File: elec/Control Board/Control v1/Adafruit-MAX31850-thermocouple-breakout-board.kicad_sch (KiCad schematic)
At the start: 20 parts

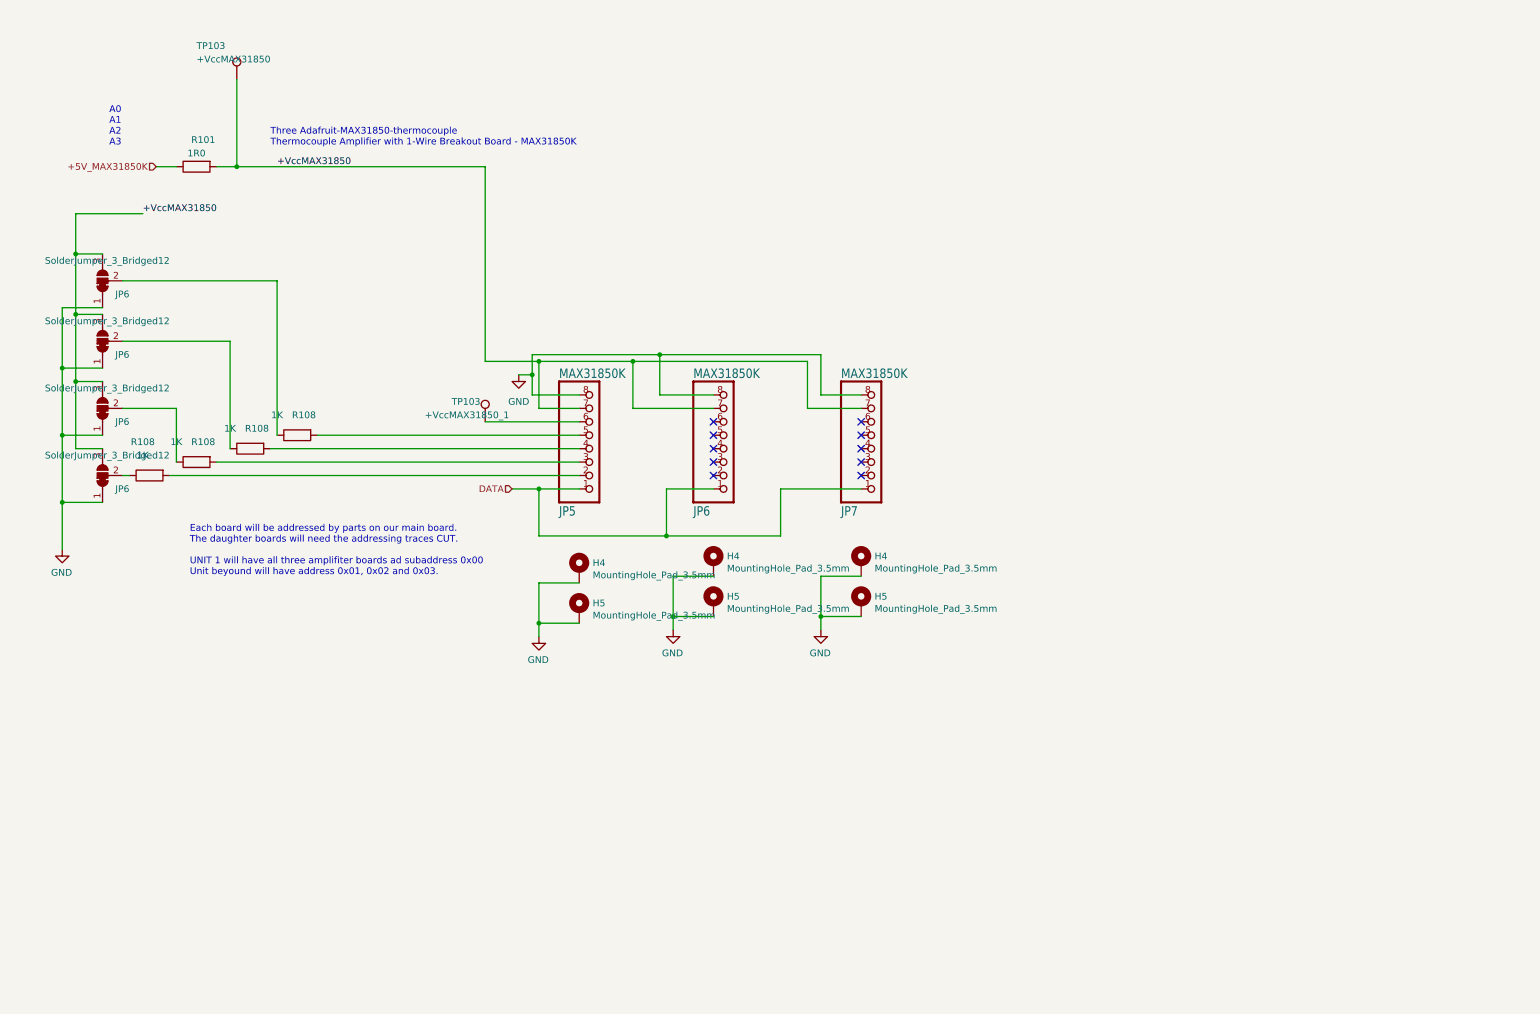
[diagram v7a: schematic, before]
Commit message: Update schematic for MCP9600 I2C thermocouple.
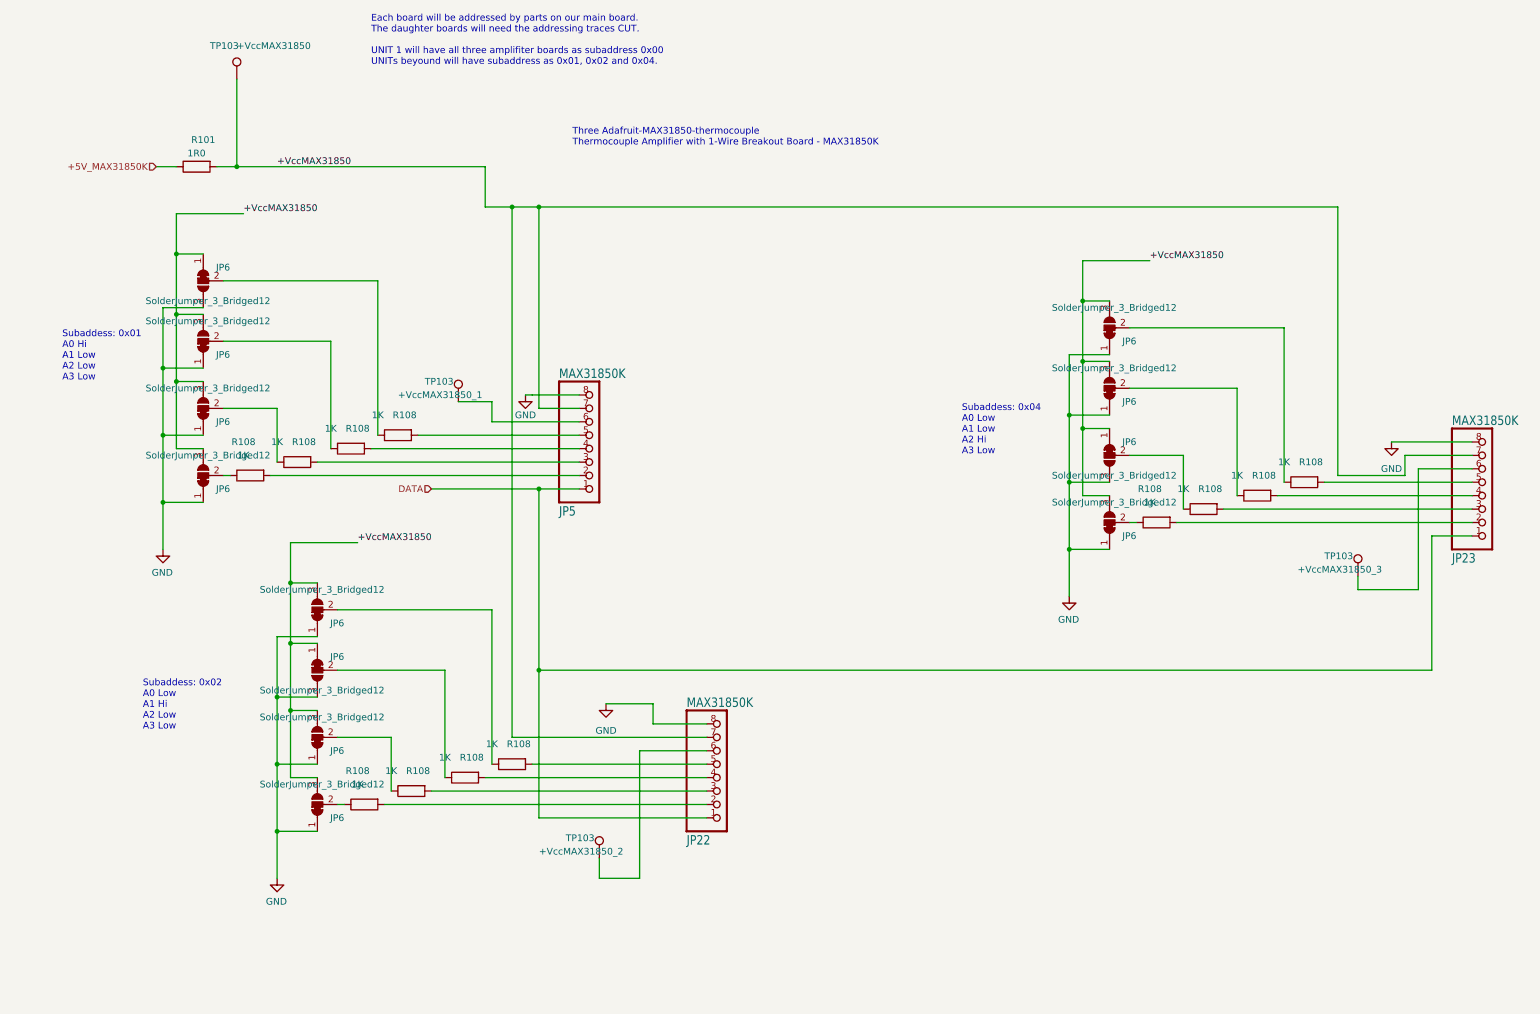
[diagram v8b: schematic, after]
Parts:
- removed H4 (x3), H5 (x3): MountingHole_Pad_3.5mm, PubInv_KiCad_PCB:MountingHole_3.5mm_Pad_Via, symbol GPAD_SCH_LIB:MountingHole_Pad_3.5mm
- removed JP6, JP7: MAX31850K, PubInv_KiCad_PCB:Adafruit_MAX31850K_Module, symbol Control v1-eagle-import:microbuilder_HEADER-1X870MIL
- added JP22, JP23: MAX31850K, PubInv_KiCad_PCB:Adafruit_MAX31850K_Module, symbol Control v1-eagle-import:microbuilder_HEADER-1X870MIL
- added JP6 (x8): SolderJumper_3_Bridged12, Jumper:SolderJumper-3_P1.3mm_Bridged12_RoundedPad1.0x1.5mm, symbol Jumper:SolderJumper_3_Bridged12
- added R108 (x8): 1K, Resistor_SMD:R_0603_1608Metric_Pad0.98x0.95mm_HandSolder, symbol Device:R
- added TP103: +VccMAX31850_2, TestPoint:TestPoint_Loop_D2.54mm_Drill1.5mm_Beaded, symbol Connector:TestPoint
- added TP103: +VccMAX31850_3, TestPoint:TestPoint_Loop_D2.54mm_Drill1.5mm_Beaded, symbol Connector:TestPoint
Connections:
- net +VccMAX31850: now also JP6.1 (A), JP22.7, JP23.7, JP6.1 (A), JP6.1 (A), JP6.3 (B), JP6.3 (B), JP6.3 (B), JP6.3 (B), JP6.3 (B), JP6.3 (B); no longer JP6.3 (B)
- net DATA: now also JP22.1, JP23.1
- net GND: now also JP6.3 (B), JP22.8, JP23.8, JP6.1 (A), JP6.1 (A), JP6.1 (A), JP6.1 (A), JP6.1 (A), JP6.1 (A), JP6.3 (B), JP6.3 (B); no longer JP6.1 (A)
- new net: JP6.2 (C), R108.1 (x8)
- new net: JP23.5, R108.2
- new net: JP23.4, R108.2
- new net: JP23.2, R108.2
- new net: JP22.6, TP103.1
- new net: JP22.5, R108.2
- new net: JP23.6, TP103.1
- new net: JP23.3, R108.2
- new net: JP22.4, R108.2
- new net: JP22.2, R108.2
- new net: JP22.3, R108.2
- no-connect marks 10 -> 0
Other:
- note added: "Each board will be addressed by parts on our main board. The daughter boards will need the addressing traces CUT. UNIT 1 will have all three amplifiter boards as subaddress 0x00 UNITs beyound will have subaddress as 0x01, 0x02 and 0x04."
- note added: "Subaddess: 0x01 A0 Hi A1 Low A2 Low A3 Low"
- note added: "Subaddess: 0x02 A0 Low A1 Hi A2 Low A3 Low"
- note added: "Subaddess: 0x04 A0 Low A1 Low A2 Hi A3 Low"
- note removed: "A0 A1 A2 A3"
- note removed: "Each board will be addressed by parts on our main board. The daughter boards will need the addressing traces CUT. UNIT 1 will have all three amplifiter boards ad subaddress 0x00 Unit beyound will have address 0x01, 0x02 and 0x03."
- moved on the sheet: JP6, R108, TP103
